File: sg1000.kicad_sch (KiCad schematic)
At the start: 66 parts, among them CN1 Conn_01x07_Female, J1 USB-B1HSB6, J2 RCJ-014, J3 RCJ-013, Q1 2n4401, Q1c1 2n3906, SW1 Pause Key, SW2 Power Toggle, U1 SG-1000-Cart, U10 PLCCZ80, U100 74HCT574, U101 74HCT574, U102 74HCT574, U103 AS6C62256-DIP, U11 AS6C62256-DIP, U12 TMS9918A, U13 74LS139, U16 74LS32, U18 74LS257, U2 SG-1000-Expansion, U21 74LS257, U3 SN76489AN, U99 74HCT04, X2 10.73863MHz

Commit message: Add test-points for 5V, GND logic probe
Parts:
- added TP2: +5V, TestPoint:TestPoint_Loop_D1.80mm_Drill1.0mm_Beaded, symbol Connector:TestPoint
- added TP3: GND, TestPoint:TestPoint_Loop_D1.80mm_Drill1.0mm_Beaded, symbol Connector:TestPoint
- gave numbers to parts that had none: 1
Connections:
- net +5V: now also TP2.1
- net GND: now also TP3.1
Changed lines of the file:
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@@
   (junction (at 76.2 127) (diameter 0) (color 0 0 0 0)
   )
+  (junction (at 344.17 59.69) (diameter 0) (color 0 0 0 0)
+  )
   (junction (at 53.34 513.08) (diameter 0) (color 0 0 0 0)
   )
@@
   (junction (at 126.365 109.22) (diameter 0) (color 0 0 0 0)
   )
+  (junction (at 320.04 59.69) (diameter 0) (color 0 0 0 0)
+  )
   (junction (at 163.83 202.565) (diameter 0) (color 0 0 0 0)
   )
@@
     (stroke (width 0) (type default) (color 0 0 0 0))
   )
+  (wire (pts (xy 320.04 59.69) (xy 320.04 68.58))
+    (stroke (width 0) (type default) (color 0 0 0 0))
+  )
   (wire (pts (xy 97.155 460.375) (xy 106.68 460.375))
     (stroke (width 0) (type default) (color 0 0 0 0))
@@
     (stroke (width 0) (type default) (color 0 0 0 0))
   )
-  (wire (pts (xy 350.52 59.69) (xy 339.09 59.69))
+  (wire (pts (xy 350.52 59.69) (xy 344.17 59.69))
     (stroke (width 0) (type default) (color 0 0 0 0))
   )
@@
     (stroke (width 0) (type default) (color 0 0 0 0))
   )
+  (wire (pts (xy 344.17 59.69) (xy 344.17 68.58))
+    (stroke (width 0) (type default) (color 0 0 0 0))
+  )
   (wire (pts (xy 99.695 398.78) (xy 65.405 398.78))
     (stroke (width 0) (type default) (color 0 0 0 0))
@@
     (stroke (width 0) (type default) (color 0 0 0 0))
   )
+  (wire (pts (xy 344.17 59.69) (xy 339.09 59.69))
+    (stroke (width 0) (type default) (color 0 0 0 0))
+  )
   (wire (pts (xy 256.54 109.22) (xy 248.285 109.22))
     (stroke (width 0) (type default) (color 0 0 0 0))
@@
   (symbol (lib_id "Jumper:SolderJumper_2_Bridged") (at 29.21 568.96 0) (unit 1)
     (in_bom yes) (on_board yes)
-    (property "Reference" "JP?" (id 0) (at 29.21 572.77 0))
+    (property "Reference" "JP4" (id 0) (at 29.21 572.77 0))
     (property "Value" "SolderJumper_2_Bridged" (id 1) (at 29.21 565.15 0)
       (effects (font (size 1.27 1.27)) hide)
@@
     (pin "2")
   )
+  (symbol (lib_id "Connector:TestPoint") (at 344.17 68.58 180) (unit 1)
+    (in_bom yes) (on_board yes)
+    (property "Reference" "TP3" (id 0) (at 346.71 70.6119 0)
+      (effects (font (size 1.27 1.27)) (justify right))
+    )
+    (property "Value" "GND" (id 1) (at 346.71 73.1519 0)
+      (effects (font (size 1.27 1.27)) (justify right))
+    )
+    (property "Footprint" "TestPoint:TestPoint_Loop_D1.80mm_Drill1.0mm_Beaded" (id 2) (at 339.09 68.58 0)
+      (effects (font (size 1.27 1.27)) hide)
+    )
+    (property "Datasheet" "~" (id 3) (at 339.09 68.58 0)
+      (effects (font (size 1.27 1.27)) hide)
+    )
+    (pin "1")
+  )
   (symbol (lib_id "power:GND") (at 124.46 567.69 0) (unit 1)
     (in_bom yes) (on_board yes) (fields_autoplaced)
@@
     (pin "1")
   )
+  (symbol (lib_id "power:GNDPWR") (at 350.52 59.69 0) (unit 1)
+    (in_bom yes) (on_board yes) (fields_autoplaced)
+    (property "Reference" "#PWR0160" (id 0) (at 350.52 64.77 0)
+      (effects (font (size 1.27 1.27)) hide)
+    )
+    (property "Value" "GNDPWR" (id 1) (at 350.393 64.77 0))
+    (property "Footprint" "" (id 2) (at 350.52 60.96 0)
+      (effects (font (size 1.27 1.27)) hide)
+    )
+    (property "Datasheet" "" (id 3) (at 350.52 60.96 0)
+      (effects (font (size 1.27 1.27)) hide)
+    )
+    (pin "1")
+  )
   (symbol (lib_id "power:+5V") (at 48.26 513.08 0) (unit 1)
     (in_bom yes) (on_board yes) (fields_autoplaced)
@@
     (pin "2")
   )
+  (symbol (lib_id "Connector:TestPoint") (at 320.04 68.58 180) (unit 1)
+    (in_bom yes) (on_board yes) (fields_autoplaced)
+    (property "Reference" "TP2" (id 0) (at 322.58 70.6119 0)
+      (effects (font (size 1.27 1.27)) (justify right))
+    )
+    (property "Value" "+5V" (id 1) (at 322.58 73.1519 0)
+      (effects (font (size 1.27 1.27)) (justify right))
+    )
+    (property "Footprint" "TestPoint:TestPoint_Loop_D1.80mm_Drill1.0mm_Beaded" (id 2) (at 314.96 68.58 0)
+      (effects (font (size 1.27 1.27)) hide)
+    )
+    (property "Datasheet" "~" (id 3) (at 314.96 68.58 0)
+      (effects (font (size 1.27 1.27)) hide)
+    )
+    (pin "1")
+  )
   (sheet_instances
     (path "/" (page "1"))
@@
       (reference "#PWR0159") (unit 1) (value "GND") (footprint "")
     )
+    (path "/bef03ebd-269a-4a00-a5ce-90ac3e0b35a9"
+      (reference "#PWR0160") (unit 1) (value "GNDPWR") (footprint "")
+    )
     (path "/00000000-0000-0000-0000-00005e7d9a30"
       (reference "C1") (unit 1) (value "0.1µF") (footprint "Capacitor_SMD:C_0805_2012Metric_Pad1.15x1.40mm_HandSolder")
@@
     )
     (path "/97d6fcd3-ceba-42ac-b87a-8d981d14ecab"
-      (reference "JP?") (unit 1) (value "SolderJumper_2_Bridged") (footprint "Jumper:SolderJumper-2_P1.3mm_Bridged_RoundedPad1.0x1.5mm")
+      (reference "JP4") (unit 1) (value "SolderJumper_2_Bridged") (footprint "Jumper:SolderJumper-2_P1.3mm_Bridged_RoundedPad1.0x1.5mm")
     )
     (path "/e8ff5aa1-c73d-405b-ae17-444be3e4dae0"
@@
       (reference "TP1") (unit 1) (value "TestPoint") (footprint "TestPoint:TestPoint_Pad_1.0x1.0mm")
     )
+    (path "/ffc04502-f2c9-488f-b0ef-6c293c75f8de"
+      (reference "TP2") (unit 1) (value "+5V") (footprint "TestPoint:TestPoint_Loop_D1.80mm_Drill1.0mm_Beaded")
+    )
+    (path "/bc415191-2264-432a-91a2-21b0cf8e7e17"
+      (reference "TP3") (unit 1) (value "GND") (footprint "TestPoint:TestPoint_Loop_D1.80mm_Drill1.0mm_Beaded")
+    )
     (path "/e4e9a9cd-894c-43a6-bbd2-9190e99d71d4"

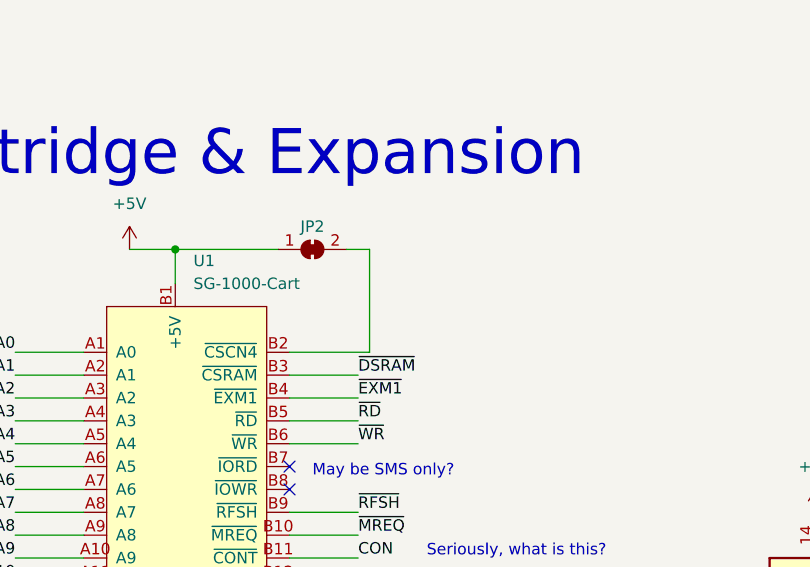
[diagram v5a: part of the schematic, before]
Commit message: CSCN4 doesn't exist on SG-1000
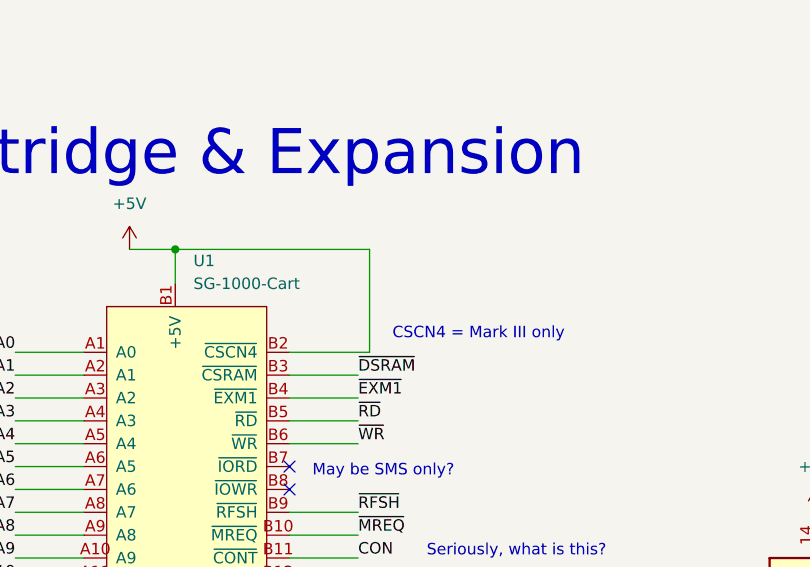
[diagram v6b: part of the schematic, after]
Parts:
- removed JP2: SolderJumper_2_Bridged, Jumper:SolderJumper-2_P1.3mm_Bridged_RoundedPad1.0x1.5mm, symbol Jumper:SolderJumper_2_Bridged
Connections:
- net +5V: now also U1.B2 (~{CSCN4})
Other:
- note added: "CSCN4 = Mark III only"
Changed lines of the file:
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@@
     (stroke (width 0) (type default) (color 0 0 0 0))
   )
+  (wire (pts (xy 53.34 513.08) (xy 74.93 513.08))
+    (stroke (width 0) (type default) (color 0 0 0 0))
+  )
   (wire (pts (xy 35.56 539.75) (xy 43.18 539.75))
     (stroke (width 0) (type default) (color 0 0 0 0))
@@
     (stroke (width 0) (type default) (color 0 0 0 0))
   )
+  (wire (pts (xy 74.93 513.08) (xy 74.93 524.51))
+    (stroke (width 0) (type default) (color 0 0 0 0))
+  )
   (wire (pts (xy 123.19 473.71) (xy 128.905 473.71))
     (stroke (width 0) (type default) (color 0 0 0 0))
@@
     (stroke (width 0) (type default) (color 0 0 0 0))
   )
-  (wire (pts (xy 64.77 513.08) (xy 53.34 513.08))
-    (stroke (width 0) (type default) (color 0 0 0 0))
-  )
   (wire (pts (xy 97.155 389.255) (xy 80.01 389.255))
     (stroke (width 0) (type default) (color 0 0 0 0))
@@
     (stroke (width 0) (type default) (color 0 0 0 0))
   )
-  (wire (pts (xy 74.93 513.08) (xy 72.39 513.08))
-    (stroke (width 0) (type default) (color 0 0 0 0))
-  )
   (wire (pts (xy 88.265 182.245) (xy 93.98 182.245))
     (stroke (width 0) (type default) (color 0 0 0 0))
@@
     (stroke (width 0) (type default) (color 0 0 0 0))
   )
-  (wire (pts (xy 74.93 524.51) (xy 74.93 513.08))
-    (stroke (width 0) (type default) (color 0 0 0 0))
-  )
   (wire (pts (xy 79.375 96.52) (xy 45.085 96.52))
     (stroke (width 0) (type default) (color 0 0 0 0))
@@
     (effects (font (size 5.0038 5.0038)) (justify left bottom))
   )
+  (text "CSCN4 = Mark III only" (at 77.47 523.24 0)
+    (effects (font (size 1.27 1.27)) (justify left bottom))
+  )
   (text "No ~{CS2} on this RAM, so no jumpers" (at 146.05 145.415 0)
     (effects (font (size 1.27 1.27)) (justify left bottom))
@@
     (pin "1")
   )
-  (symbol (lib_id "Jumper:SolderJumper_2_Bridged") (at 68.58 513.08 0) (unit 1)
-    (in_bom yes) (on_board yes)
-    (property "Reference" "JP2" (id 0) (at 68.58 510.54 0))
-    (property "Value" "SolderJumper_2_Bridged" (id 1) (at 68.58 509.27 0)
-      (effects (font (size 1.27 1.27)) hide)
-    )
-    (property "Footprint" "Jumper:SolderJumper-2_P1.3mm_Bridged_RoundedPad1.0x1.5mm" (id 2) (at 68.58 513.08 0)
-      (effects (font (size 1.27 1.27)) hide)
-    )
-    (property "Datasheet" "~" (id 3) (at 68.58 513.08 0)
-      (effects (font (size 1.27 1.27)) hide)
-    )
-    (pin "1")
-    (pin "2")
-  )
   (symbol (lib_id "Device:C_Small") (at 281.94 205.74 90) (unit 1)
     (in_bom yes) (on_board yes) (fields_autoplaced)
@@
       (reference "JP1") (unit 1) (value "SolderJumper_2_Open") (footprint "Jumper:SolderJumper-2_P1.3mm_Open_RoundedPad1.0x1.5mm")
     )
-    (path "/fc0aae14-e17d-492d-9c8a-69738a138609"
-      (reference "JP2") (unit 1) (value "SolderJumper_2_Bridged") (footprint "Jumper:SolderJumper-2_P1.3mm_Bridged_RoundedPad1.0x1.5mm")
-    )
     (path "/abb8dd2a-03fb-4e18-ac16-ae57c97f0ae6"

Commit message: Add NMI test point
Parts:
- removed JP1: SolderJumper_2_Open, Jumper:SolderJumper-2_P1.3mm_Open_RoundedPad1.0x1.5mm, symbol Jumper:SolderJumper_2_Open
- removed JP4: SolderJumper_2_Bridged, Jumper:SolderJumper-2_P1.3mm_Bridged_RoundedPad1.0x1.5mm, symbol Jumper:SolderJumper_2_Bridged
- added TP?: ~{NMI}, TestPoint:TestPoint_Pad_1.0x1.0mm, symbol Connector:TestPoint
- TP1: value TestPoint -> ~{HALT}
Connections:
- net ~{EXM2}: now also U1.B19 (~{EXM2})
- net ~{NMI}: now also TP?.1
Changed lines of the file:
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@@
   (junction (at 284.48 181.61) (diameter 0) (color 0 0 0 0)
   )
-  (junction (at 168.275 81.28) (diameter 0) (color 0 0 0 0)
-  )
   (junction (at 97.155 389.255) (diameter 0) (color 0 0 0 0)
   )
@@
   (junction (at 106.68 460.375) (diameter 0) (color 0 0 0 0)
   )
-  (junction (at 38.1 562.61) (diameter 0) (color 0 0 0 0)
-  )
   (junction (at 126.365 109.22) (diameter 0) (color 0 0 0 0)
   )
@@
     (stroke (width 0) (type default) (color 0 0 0 0))
   )
-  (wire (pts (xy 255.905 91.44) (xy 248.285 91.44))
+  (wire (pts (xy 248.285 91.44) (xy 264.16 91.44))
     (stroke (width 0) (type default) (color 0 0 0 0))
   )
@@
     (stroke (width 0) (type default) (color 0 0 0 0))
   )
-  (wire (pts (xy 22.86 568.96) (xy 25.4 568.96))
-    (stroke (width 0) (type default) (color 0 0 0 0))
-  )
   (wire (pts (xy 45.085 365.76) (xy 52.705 365.76))
     (stroke (width 0) (type default) (color 0 0 0 0))
@@
     (stroke (width 0) (type default) (color 0 0 0 0))
   )
-  (wire (pts (xy 168.275 81.28) (xy 170.18 81.28))
+  (wire (pts (xy 167.005 81.28) (xy 170.18 81.28))
     (stroke (width 0) (type default) (color 0 0 0 0))
   )
@@
     (stroke (width 0) (type default) (color 0 0 0 0))
   )
-  (wire (pts (xy 33.02 568.96) (xy 38.1 568.96))
-    (stroke (width 0) (type default) (color 0 0 0 0))
-  )
   (wire (pts (xy 92.075 379.095) (xy 92.075 371.475))
     (stroke (width 0) (type default) (color 0 0 0 0))
@@
     (stroke (width 0) (type default) (color 0 0 0 0))
   )
-  (wire (pts (xy 38.1 568.96) (xy 38.1 562.61))
-    (stroke (width 0) (type default) (color 0 0 0 0))
-  )
   (wire (pts (xy 111.125 120.015) (xy 102.87 120.015))
     (stroke (width 0) (type default) (color 0 0 0 0))
@@
     (stroke (width 0) (type default) (color 0 0 0 0))
   )
-  (wire (pts (xy 22.86 562.61) (xy 25.4 562.61))
-    (stroke (width 0) (type default) (color 0 0 0 0))
-  )
   (bus (pts (xy 135.255 76.2) (xy 135.255 78.74))
     (stroke (width 0) (type default) (color 0 0 0 0))
@@
     (stroke (width 0) (type default) (color 0 0 0 0))
   )
-  (wire (pts (xy 170.18 84.455) (xy 168.275 84.455))
-    (stroke (width 0) (type default) (color 0 0 0 0))
-  )
   (wire (pts (xy 35.56 590.55) (xy 43.18 590.55))
     (stroke (width 0) (type default) (color 0 0 0 0))
@@
     (stroke (width 0) (type default) (color 0 0 0 0))
   )
-  (wire (pts (xy 38.1 562.61) (xy 43.18 562.61))
+  (wire (pts (xy 35.56 562.61) (xy 43.18 562.61))
     (stroke (width 0) (type default) (color 0 0 0 0))
   )
@@
     (stroke (width 0) (type default) (color 0 0 0 0))
   )
-  (wire (pts (xy 168.275 84.455) (xy 168.275 81.28))
-    (stroke (width 0) (type default) (color 0 0 0 0))
-  )
   (wire (pts (xy 34.29 453.39) (xy 40.005 453.39))
     (stroke (width 0) (type default) (color 0 0 0 0))
@@
     (stroke (width 0) (type default) (color 0 0 0 0))
   )
-  (wire (pts (xy 168.275 81.28) (xy 167.005 81.28))
-    (stroke (width 0) (type default) (color 0 0 0 0))
-  )
   (wire (pts (xy 144.145 119.38) (xy 142.24 119.38))
     (stroke (width 0) (type default) (color 0 0 0 0))
@@
     (stroke (width 0) (type default) (color 0 0 0 0))
   )
+  (wire (pts (xy 264.16 87.63) (xy 264.16 91.44))
+    (stroke (width 0) (type default) (color 0 0 0 0))
+  )
   (wire (pts (xy 262.89 138.43) (xy 273.685 138.43))
     (stroke (width 0) (type default) (color 0 0 0 0))
@@
     (stroke (width 0) (type default) (color 0 0 0 0))
   )
-  (wire (pts (xy 33.02 562.61) (xy 38.1 562.61))
-    (stroke (width 0) (type default) (color 0 0 0 0))
-  )
   (wire (pts (xy 43.815 422.91) (xy 52.705 422.91))
     (stroke (width 0) (type default) (color 0 0 0 0))
@@
     (effects (font (size 1.27 1.27)) (justify right bottom))
   )
-  (label "~{DSRAM}" (at 170.18 81.28 0)
-    (effects (font (size 1.27 1.27)) (justify left bottom))
-  )
   (label "AD3" (at 226.06 250.19 180)
     (effects (font (size 1.27 1.27)) (justify right bottom))
@@
     (effects (font (size 1.27 1.27)) (justify right bottom))
   )
-  (label "A15" (at 22.86 562.61 180)
-    (effects (font (size 1.27 1.27)) (justify right bottom))
-  )
   (label "A7" (at 34.29 106.045 180)
     (effects (font (size 1.27 1.27)) (justify right bottom))
@@
     (effects (font (size 1.27 1.27)) (justify left bottom))
   )
-  (label "~{CS_WRAM}" (at 170.18 84.455 0)
+  (label "~{CS_WRAM}" (at 170.18 81.28 0)
     (effects (font (size 1.27 1.27)) (justify left bottom))
   )
@@
     (effects (font (size 1.27 1.27)) (justify left bottom))
   )
-  (label "~{EXM2}" (at 22.86 568.96 180)
+  (label "~{EXM2}" (at 35.56 562.61 180)
     (effects (font (size 1.27 1.27)) (justify right bottom))
   )
@@
     (effects (font (size 1.27 1.27)) (justify right bottom))
   )
-  (label "~{DSRAM}" (at 73.66 527.05 0)
+  (label "~{CS_WRAM}" (at 73.66 527.05 0)
     (effects (font (size 1.27 1.27)) (justify left bottom))
   )
@@
       (effects (font (size 1.27 1.27)) (justify left))
     )
-    (property "Value" "TestPoint" (id 1) (at 268.1732 93.2942 0)
+    (property "Value" "~{HALT}" (id 1) (at 268.1732 93.2942 0)
       (effects (font (size 1.27 1.27)) (justify left))
     )
@@
     (pin "9")
   )
-  (symbol (lib_id "Jumper:SolderJumper_2_Open") (at 29.21 562.61 0) (unit 1)
-    (in_bom yes) (on_board yes)
-    (property "Reference" "JP1" (id 0) (at 29.21 565.15 0))
-    (property "Value" "SolderJumper_2_Open" (id 1) (at 29.21 558.8 0)
-      (effects (font (size 1.27 1.27)) hide)
-    )
-    (property "Footprint" "Jumper:SolderJumper-2_P1.3mm_Open_RoundedPad1.0x1.5mm" (id 2) (at 29.21 562.61 0)
-      (effects (font (size 1.27 1.27)) hide)
-    )
-    (property "Datasheet" "~" (id 3) (at 29.21 562.61 0)
-      (effects (font (size 1.27 1.27)) hide)
-    )
-    (pin "1")
-    (pin "2")
-  )
   (symbol (lib_id "power:+5V") (at 234.95 234.95 0) (unit 1)
     (in_bom yes) (on_board yes) (fields_autoplaced)
@@
     (pin "1")
   )
-  (symbol (lib_id "Jumper:SolderJumper_2_Bridged") (at 29.21 568.96 0) (unit 1)
-    (in_bom yes) (on_board yes)
-    (property "Reference" "JP4" (id 0) (at 29.21 572.77 0))
-    (property "Value" "SolderJumper_2_Bridged" (id 1) (at 29.21 565.15 0)
-      (effects (font (size 1.27 1.27)) hide)
-    )
-    (property "Footprint" "Jumper:SolderJumper-2_P1.3mm_Bridged_RoundedPad1.0x1.5mm" (id 2) (at 29.21 568.96 0)
-      (effects (font (size 1.27 1.27)) hide)
-    )
-    (property "Datasheet" "~" (id 3) (at 29.21 568.96 0)
-      (effects (font (size 1.27 1.27)) hide)
-    )
-    (pin "1")
-    (pin "2")
-  )
   (symbol (lib_id "Device:R_Small_US") (at 284.48 185.42 0) (unit 1)
     (in_bom yes) (on_board yes) (fields_autoplaced)
@@
     (pin "2")
   )
+  (symbol (lib_id "Connector:TestPoint") (at 264.16 87.63 0) (unit 1)
+    (in_bom yes) (on_board yes) (fields_autoplaced)
+    (property "Reference" "TP?" (id 0) (at 266.7 83.0579 0)
+      (effects (font (size 1.27 1.27)) (justify left))
+    )
+    (property "Value" "~{NMI}" (id 1) (at 266.7 86.2329 0)
+      (effects (font (size 1.27 1.27)) (justify left))
+    )
+    (property "Footprint" "TestPoint:TestPoint_Pad_1.0x1.0mm" (id 2) (at 269.24 87.63 0)
+      (effects (font (size 1.27 1.27)) hide)
+    )
+    (property "Datasheet" "~" (id 3) (at 269.24 87.63 0)
+      (effects (font (size 1.27 1.27)) hide)
+    )
+    (pin "1")
+  )
   (symbol (lib_id "Connector:TestPoint") (at 344.17 68.58 180) (unit 1)
     (in_bom yes) (on_board yes)
@@
       (reference "JOY2") (unit 1) (value "DB9_Female") (footprint "LeadedSolder:A-DS 09 A-KG-T2S")
     )
-    (path "/5c331895-bde6-435d-bdc1-a0c6b91a4f03"
-      (reference "JP1") (unit 1) (value "SolderJumper_2_Open") (footprint "Jumper:SolderJumper-2_P1.3mm_Open_RoundedPad1.0x1.5mm")
-    )
     (path "/abb8dd2a-03fb-4e18-ac16-ae57c97f0ae6"
       (reference "JP3") (unit 1) (value "Jumper_2_Bridged") (footprint "Jumper:SolderJumper-2_P1.3mm_Bridged2Bar_RoundedPad1.0x1.5mm")
     )
-    (path "/97d6fcd3-ceba-42ac-b87a-8d981d14ecab"
-      (reference "JP4") (unit 1) (value "SolderJumper_2_Bridged") (footprint "Jumper:SolderJumper-2_P1.3mm_Bridged_RoundedPad1.0x1.5mm")
-    )
     (path "/e8ff5aa1-c73d-405b-ae17-444be3e4dae0"
       (reference "Q1") (unit 1) (value "2n4401") (footprint "Package_TO_SOT_THT:TO-92_Inline_Wide")
@@
     )
     (path "/00000000-0000-0000-0000-0000621835e6"
-      (reference "TP1") (unit 1) (value "TestPoint") (footprint "TestPoint:TestPoint_Pad_1.0x1.0mm")
+      (reference "TP1") (unit 1) (value "~{HALT}") (footprint "TestPoint:TestPoint_Pad_1.0x1.0mm")
     )
     (path "/ffc04502-f2c9-488f-b0ef-6c293c75f8de"
@@
       (reference "TP3") (unit 1) (value "GND") (footprint "TestPoint:TestPoint_Loop_D1.80mm_Drill1.0mm_Beaded")
     )
+    (path "/b71eafdc-9c03-445b-8de6-c72ccf90805a"
+      (reference "TP?") (unit 1) (value "~{NMI}") (footprint "TestPoint:TestPoint_Pad_1.0x1.0mm")
+    )
     (path "/e4e9a9cd-894c-43a6-bbd2-9190e99d71d4"
